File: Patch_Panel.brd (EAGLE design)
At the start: 128.3 x 222.2 mm, 43 parts, among them M1_IN APP_2POS_CONFIGMOCO_VERT, M1_OUT APP_2POS_CONFIGMOCO_VERT_DUMMY, M2_IN APP_2POS_CONFIGMOCO_VERT, M2_OUT APP_2POS_CONFIGMOCO_VERT_DUMMY, M3_IN APP_2POS_CONFIGMOCO_VERT, M3_OUT APP_2POS_CONFIGMOCO_VERT_DUMMY, M4_IN APP_2POS_CONFIGMOCO_VERT, M4_OUT APP_2POS_CONFIGMOCO_VERT_DUMMY, M5_IN APP_2POS_CONFIGMOCO_VERT, M5_OUT APP_2POS_CONFIGMOCO_VERT_DUMMY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

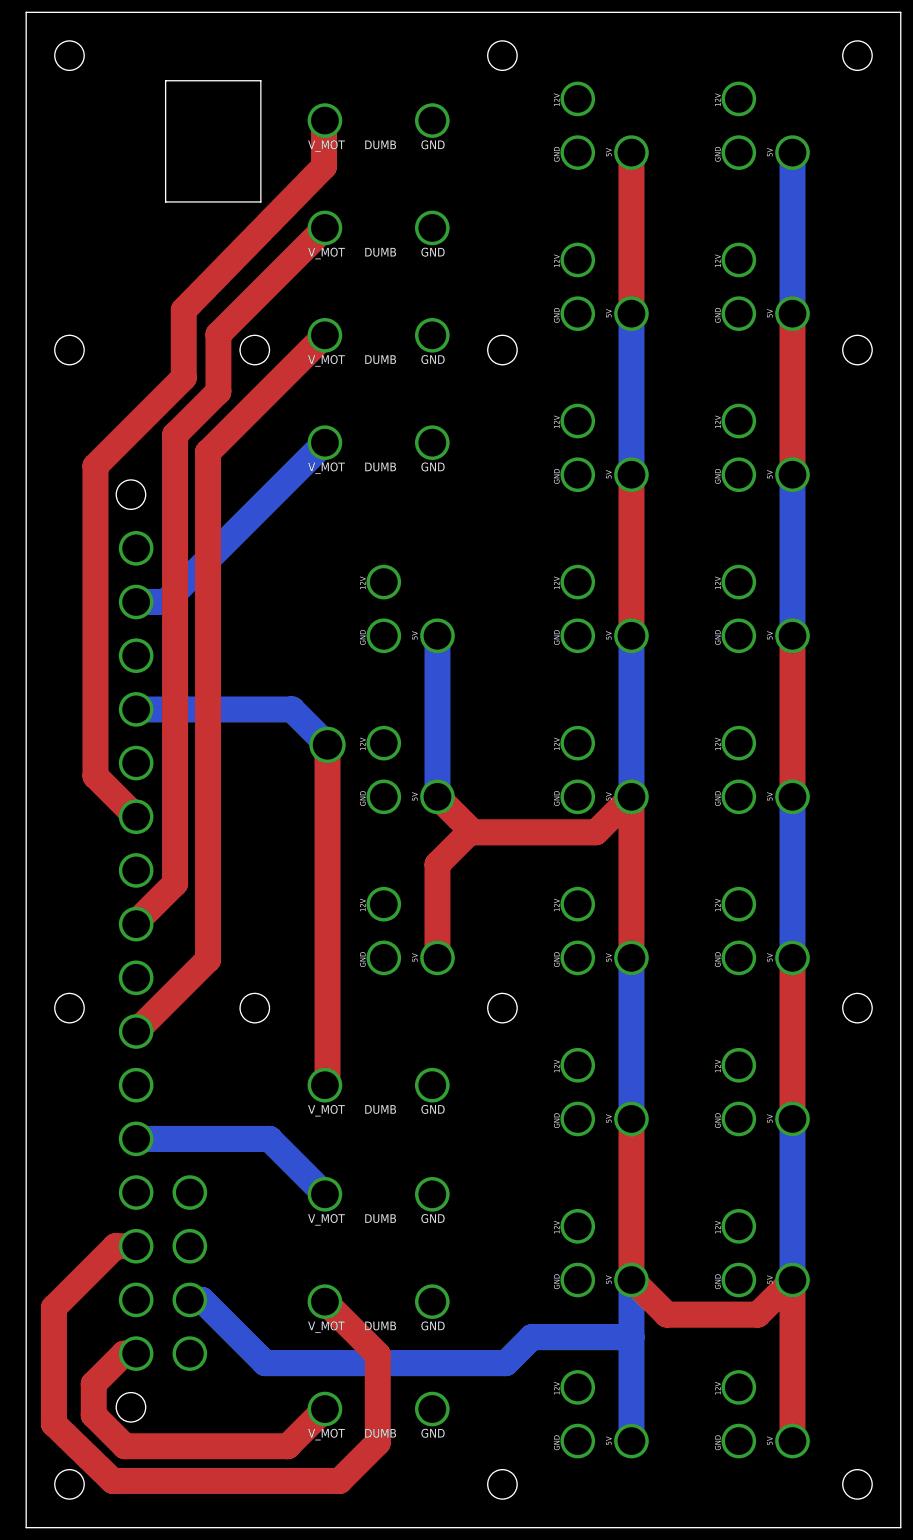
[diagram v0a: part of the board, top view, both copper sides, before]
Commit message: added cutout, rerouted w/ vert app connectors for power in
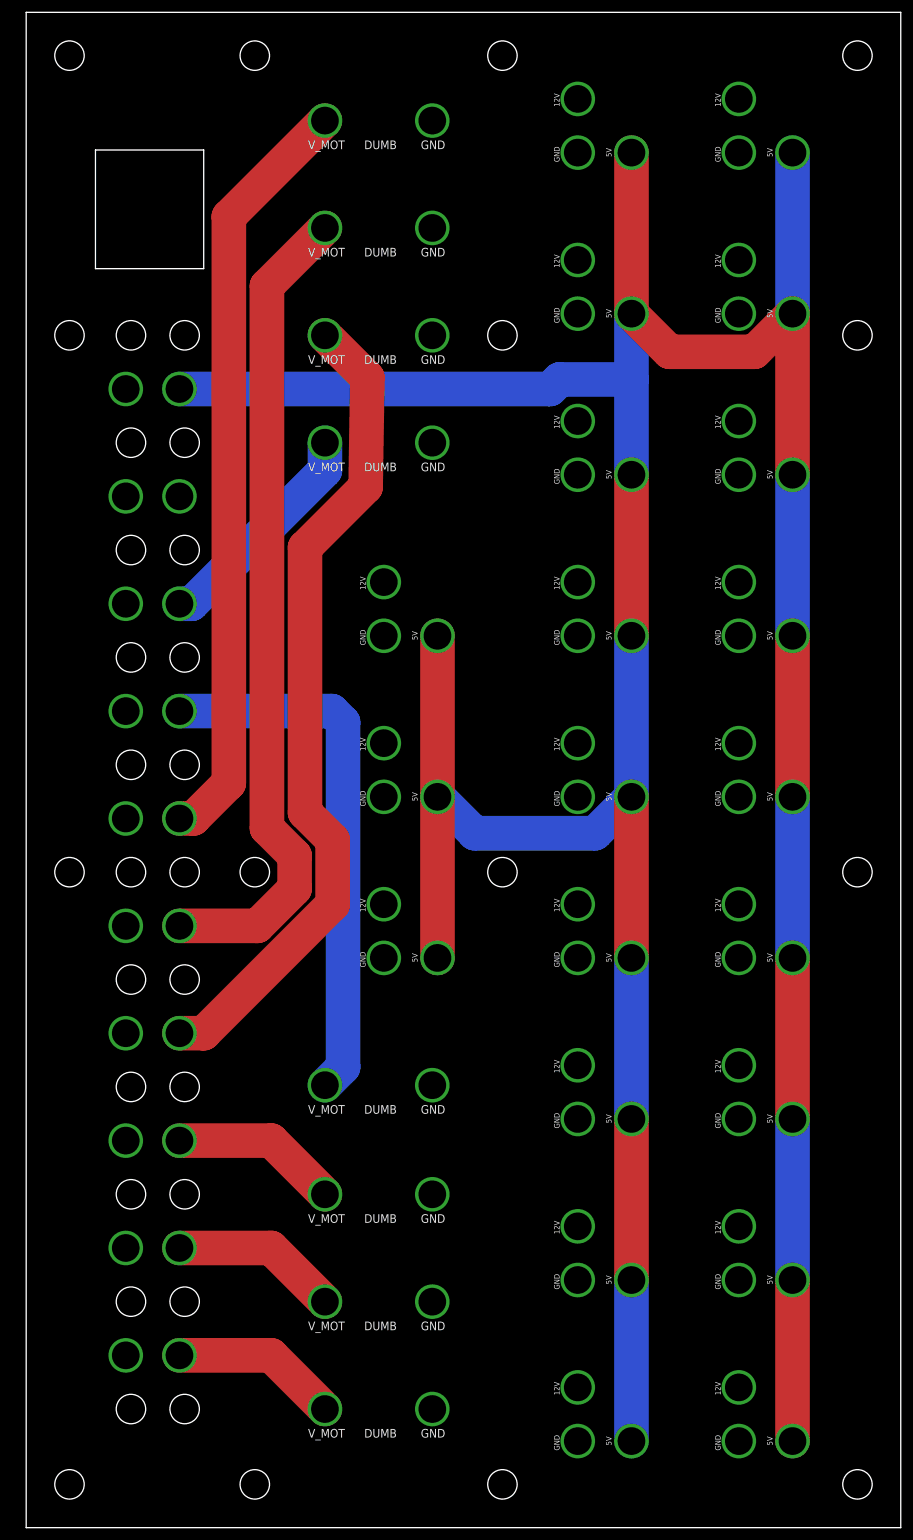
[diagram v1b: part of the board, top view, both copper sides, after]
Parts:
- added U$22, U$29, U$30, U$31, U$32, U$33, U$34, U$35, U$36, U$37, U$38, U$39, U$40, U$41, U$42, U$43, U$44, U$45: APP_MOUTING_WINGVERT, MRDT-Connectors:APP45_MOUNTING_WING_VERT
- added U$46: RJ45_PASSTHRUSTEWART-SS82000002, MRDT-Connectors:RJ45_PT_STEWART-SS82000002
- U$10, U$9: device MRDT-Connectors:PP_MOUNTING_WING_VERT -> MRDT-Connectors:APP45_MOUNTING_WING_VERT
- U$25, U$26: value ANDERSON_POWERPOLEPP45_PCB_VERT -> APP_2POS_CONFIGMOCO_VERT; device MRDT-Connectors:PP45_PCB_VERT -> MRDT-Connectors:APP45_MOCO_VERT_CONFIG
- U$27, U$28: value ANDERSON_POWERPOLEPP45_PCB_VERT -> APP_MOUTING_WINGVERT; device MRDT-Connectors:PP45_PCB_VERT -> MRDT-Connectors:APP45_MOUNTING_WING_VERT
- moved U$26 134.5 mm to (11.4, 163.1), turned to 90 degrees
- moved U$25 103.3 mm to (11.4, 147.3), turned to 90 degrees
- moved U$27 71.0 mm to (19.3, 123.7), turned to 90 degrees
- moved U$28 55.4 mm to (19.3, 92.2), turned to 90 degrees
- moved U$10 32.7 mm to (11.4, 123.7), turned to 90 degrees
- moved AUX2_IN 17.8 mm to (11.4, 131.6), turned to 90 degrees
- moved M6_IN 17.8 mm to (11.4, 100.1), turned to 90 degrees
- moved M1_IN 17.8 mm to (11.4, 21.3), turned to 90 degrees
- moved M3_IN 17.8 mm to (11.4, 52.8), turned to 90 degrees
- moved AUX1_IN 17.8 mm to (11.4, 115.8), turned to 90 degrees
- moved M2_IN 17.8 mm to (11.4, 37.1), turned to 90 degrees
- moved M4_IN 17.8 mm to (11.4, 68.6), turned to 90 degrees
- moved M5_IN 17.8 mm to (11.4, 84.3), turned to 90 degrees
- moved U$9 11.3 mm to (11.4, 13.5), turned to 90 degrees
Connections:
- net 12V: now also U$25.VCC; no longer U$27.P$1
- net 5V: now also U$26.VCC; no longer U$28.P$1
- net GND: now also U$25.GND, U$26.GND; no longer U$25.P$1, U$26.P$1
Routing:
- net M2_VCC: track 109.9 -> 24.6 mm
- net M1_VCC: track 50.7 -> 24.6 mm
- net M4_VCC: track 113.6 -> 121.7 mm
- net M5_VCC: track 113.6 -> 121.3 mm
- net M3_VCC: track 31.1 -> 24.6 mm
- net M6_VCC: track 118.4 -> 112.4 mm
- net AUX2_VCC: track 37.4 -> 33.5 mm
- net AUX1_VCC: track 80.3 -> 79.0 mm, vias 1 -> 0
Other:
- outline, holes or cut-outs redrawn
- board text removed: "12V_REG"
- board text removed: "5V_REG"
- board text removed: "GND"

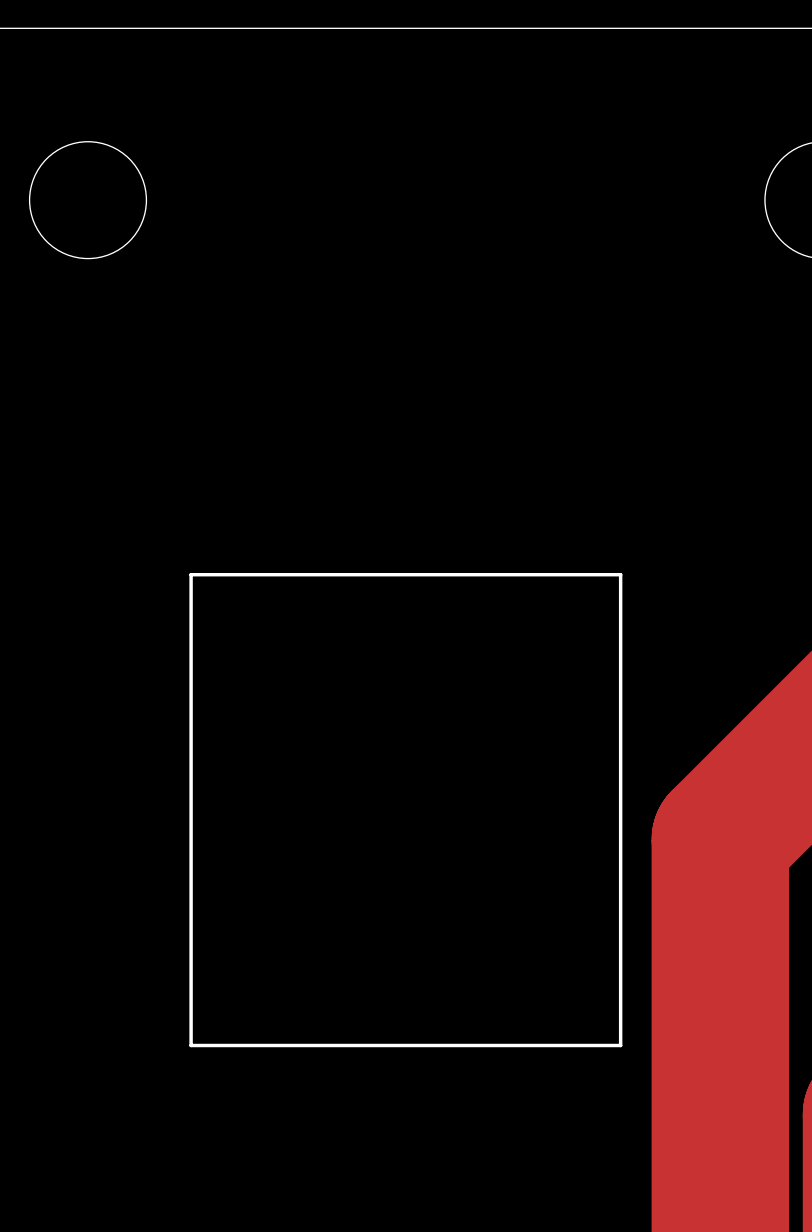
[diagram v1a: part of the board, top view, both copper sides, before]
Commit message: added rj45 standoff - needs placed
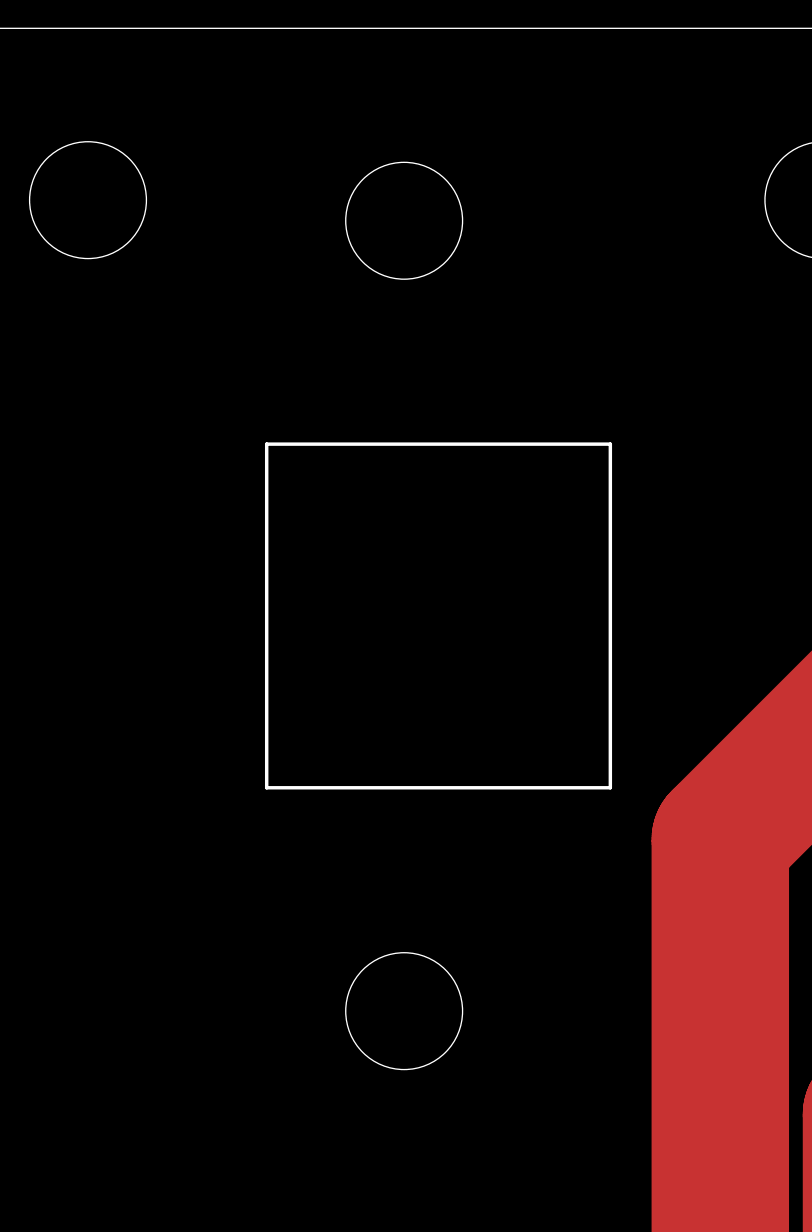
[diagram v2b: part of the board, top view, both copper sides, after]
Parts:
- U$46: value RJ45_PASSTHRUSTEWART-SS82000002 -> RJ45_PASSTHRUMRDT_MALE_RJ45_STANDOFF; device MRDT-Connectors:RJ45_PT_STEWART-SS82000002 -> MRDT-Connectors:MRDT_MALE_RJ45_STANDOFF
- moved U$46 27.9 mm to (10.4, 212.6), turned to 270 degrees
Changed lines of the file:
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@@
 <attribute name="COLOR1" value="" x="19.304" y="139.446" size="1.778" layer="28" rot="MR90" display="off"/>
 </element>
-<element name="U$46" library="MRDT-Connectors" package="RJ45_PT_STEWART-SS82000002" value="RJ45_PASSTHRUSTEWART-SS82000002" x="10.16" y="184.658">
-<attribute name="MFR" value="Stewart Connectors" x="10.16" y="184.658" size="1.778" layer="27" display="off"/>
-<attribute name="MFR_PN" value="SS-82000-002" x="10.16" y="184.658" size="1.778" layer="27" display="off"/>
-</element>
+<element name="U$46" library="MRDT-Connectors" package="MRDT_MALE_RJ45_STANDOFF" value="RJ45_PASSTHRUMRDT_MALE_RJ45_STANDOFF" x="10.414" y="212.598" rot="R270"/>
 </elements>
 <signals>

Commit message: github sucks. i changed some stuff
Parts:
- added U$47, U$48, U$49, U$50, U$52, U$53, U$54, U$55, U$56, U$57, U$58, U$59, U$60, U$61: MOUNTING_HOLE#8, MRDT-Hardware:#8_SCREW
- moved AUX1_IN 8.89 mm to (2.54, 115.8)
- moved AUX1_OUT 8.89 mm to (54.6, 68.1)
- moved AUX2_IN 8.89 mm to (2.54, 131.6)
- moved AUX2_OUT 8.89 mm to (54.6, 162.3)
- moved M1_IN 8.89 mm to (2.54, 21.3)
- moved M1_OUT 8.89 mm to (54.6, 20.6)
- moved M2_IN 8.89 mm to (2.54, 37.1)
- moved M2_OUT 8.89 mm to (54.6, 36.3)
- moved M3_IN 8.89 mm to (2.54, 52.8)
- moved M3_OUT 8.89 mm to (54.6, 52.1)
- moved M4_IN 8.89 mm to (2.54, 68.6)
- moved M4_OUT 8.89 mm to (54.6, 178.1)
- moved M5_IN 8.89 mm to (2.54, 84.3)
- moved M5_OUT 8.89 mm to (54.6, 193.8)
- moved M6_IN 8.89 mm to (2.54, 100.1)
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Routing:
- net M6_VCC: track 112.4 -> 148.5 mm
- net M4_VCC: track 121.7 -> 118.4 mm
- net 5V: track 553.2 -> 553.7 mm
- added copper zone on layer 1, net M6_VCC
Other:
- board size 128.3 x 222.2 mm -> 119.4 x 222.2 mm
